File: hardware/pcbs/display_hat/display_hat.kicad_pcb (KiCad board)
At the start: 2 copper layers, 31 x 65 mm, 13 parts, among them J1 WAVESHARE_HAT_HEADER, J2 MTA100_08, J3 MTA100_08, J4 MTA100_02

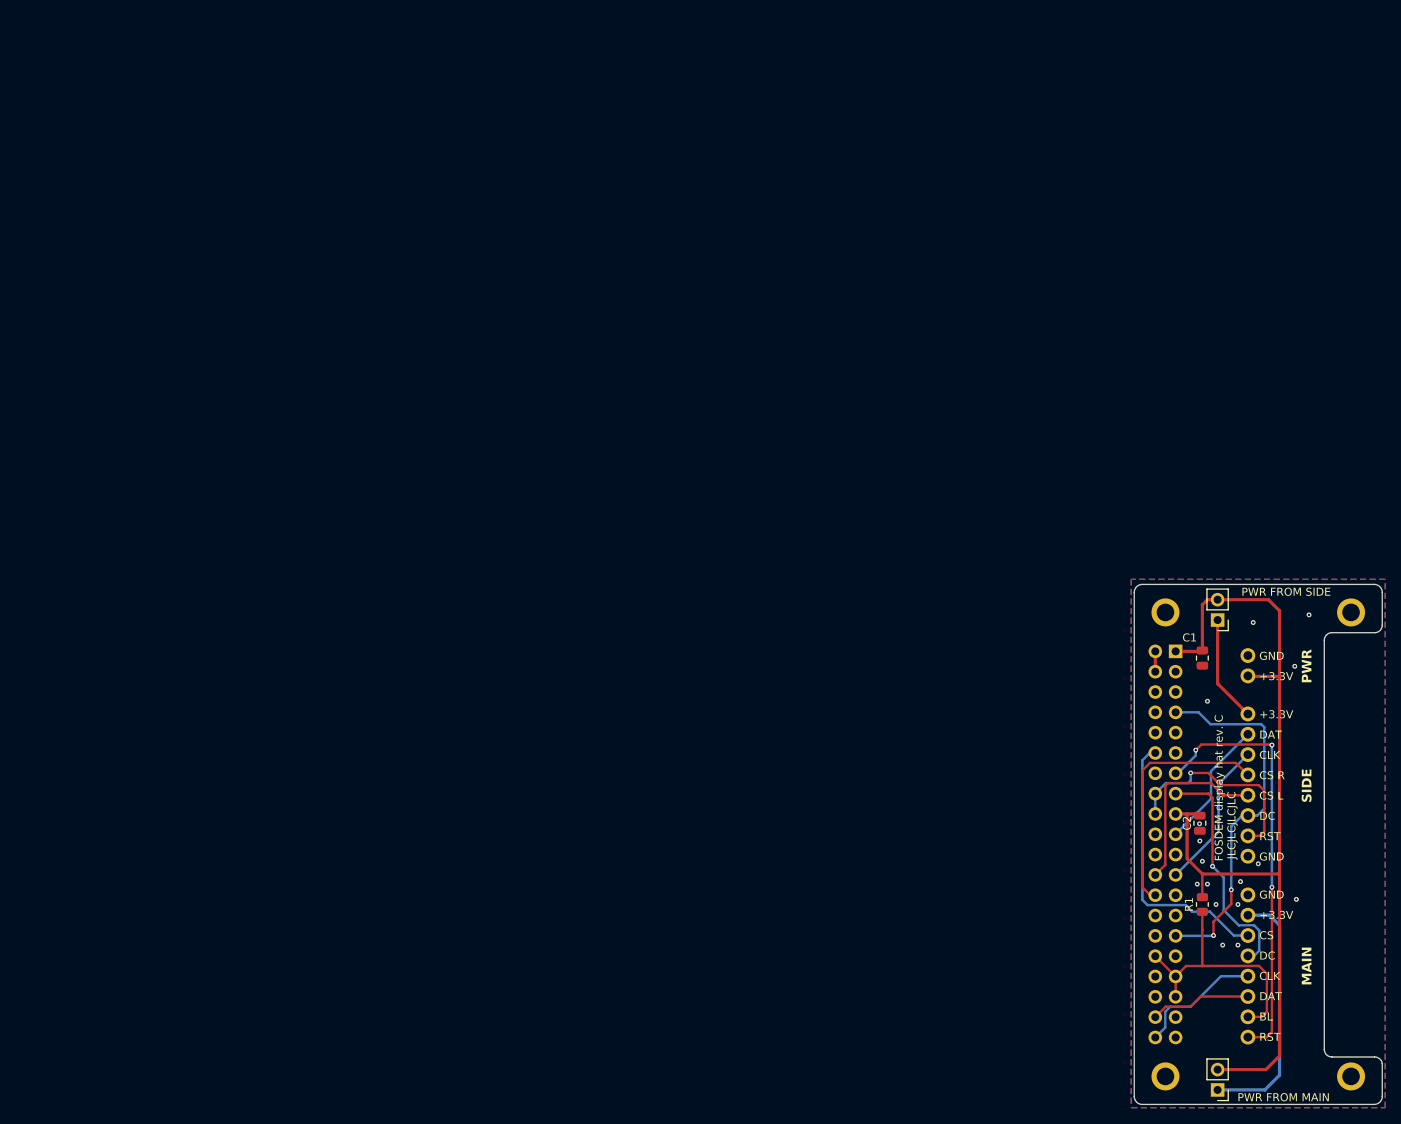
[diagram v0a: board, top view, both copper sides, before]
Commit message: baseplate: show 3D models of hat PCBs
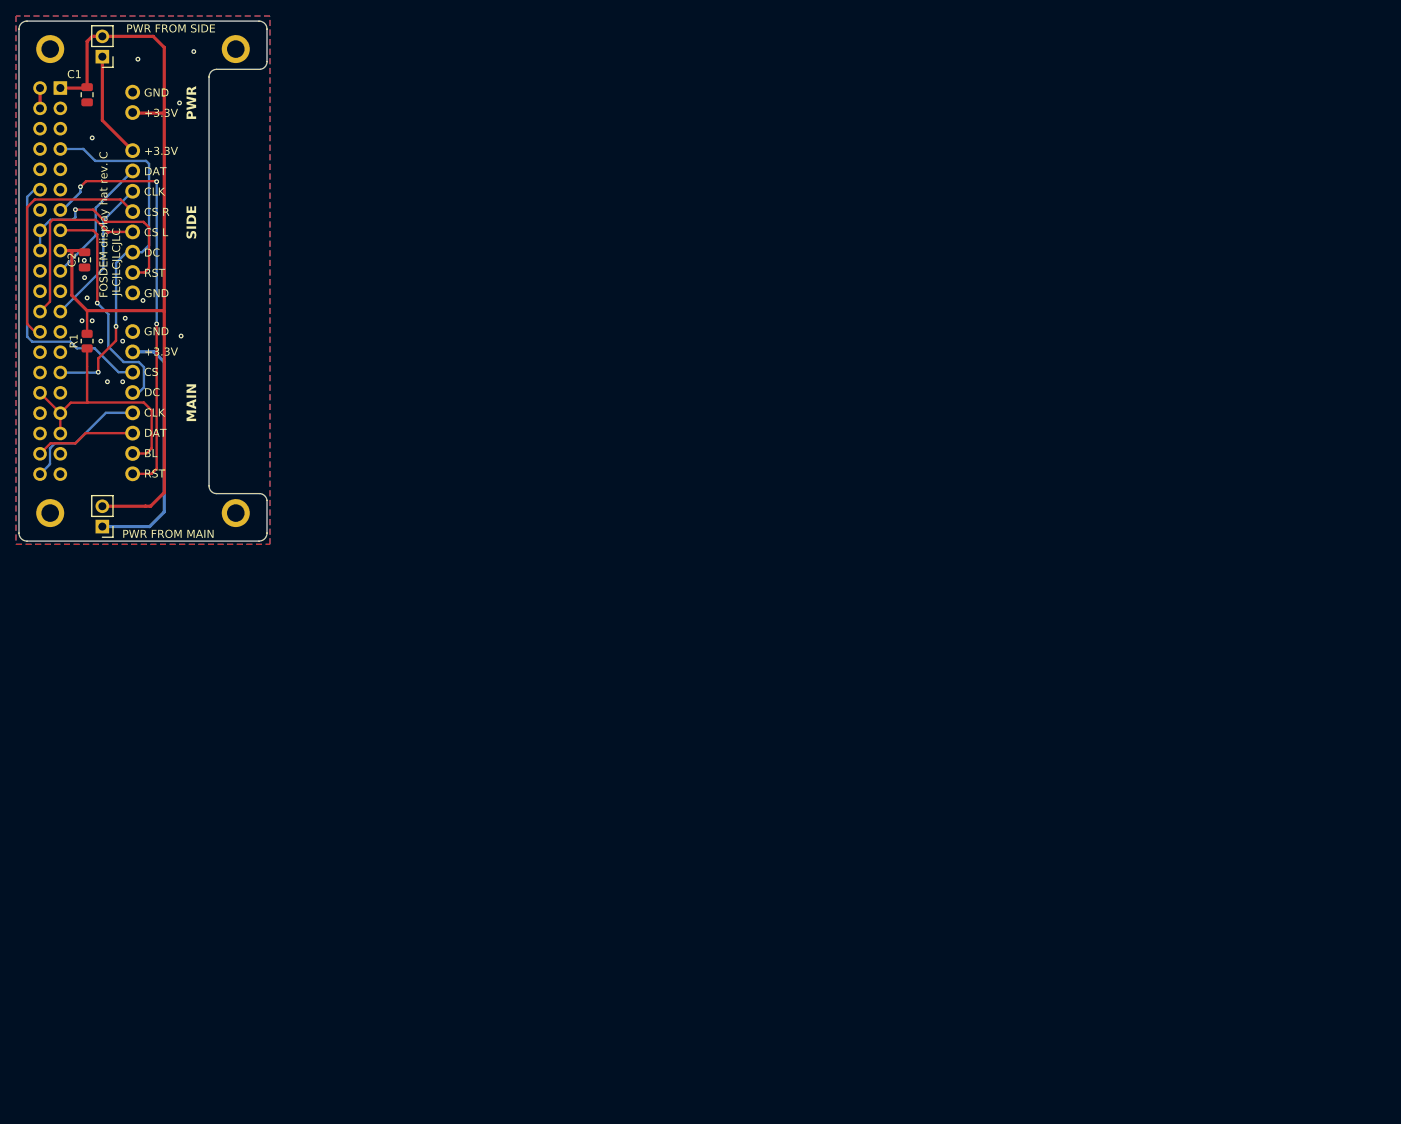
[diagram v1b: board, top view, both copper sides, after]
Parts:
- moved C1 156.2 mm to (4.62, 5.71)
- moved C2 156.2 mm to (4.30, 26.3)
- moved H1 156.2 mm to (23.2, 58.0)
- moved H2 156.2 mm to (0.00, 0.00)
- moved H3 156.2 mm to (23.2, 0.00)
- moved H4 156.2 mm to (0.00, 58.0)
- moved J1 156.2 mm to (1.27, 4.87)
- moved J2 156.2 mm to (10.3, 12.7)
- moved J3 156.2 mm to (10.3, 35.3)
- moved J4 156.2 mm to (10.3, 5.39)
- moved JP1 156.2 mm to (6.52, 0.95)
- moved JP2 156.2 mm to (6.52, 59.7)
- moved R1 156.2 mm to (4.62, 36.5)

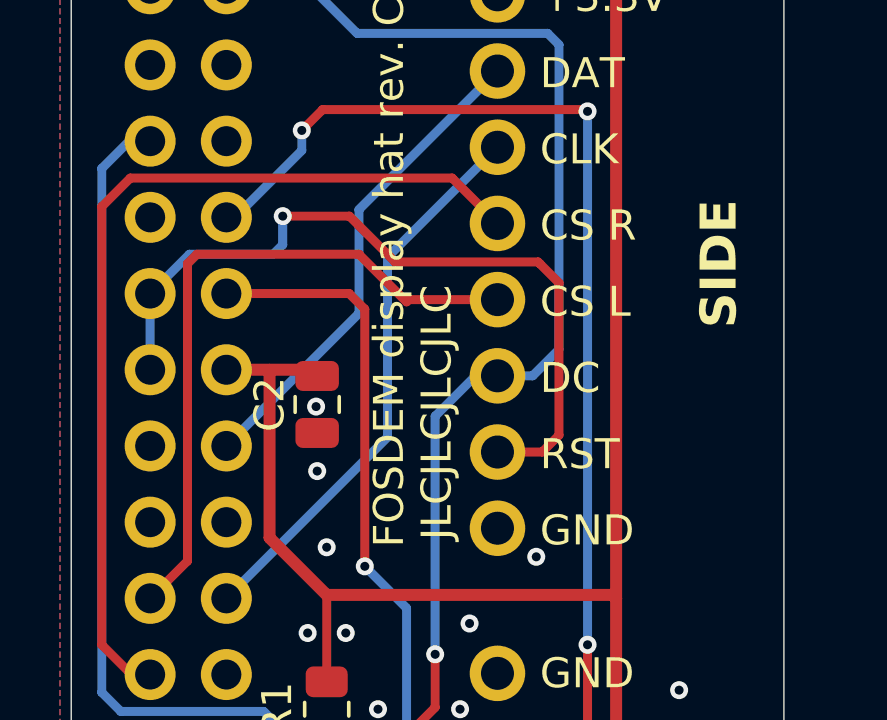
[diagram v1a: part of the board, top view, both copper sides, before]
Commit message: boards: fix minor mistakes and aisler IDs
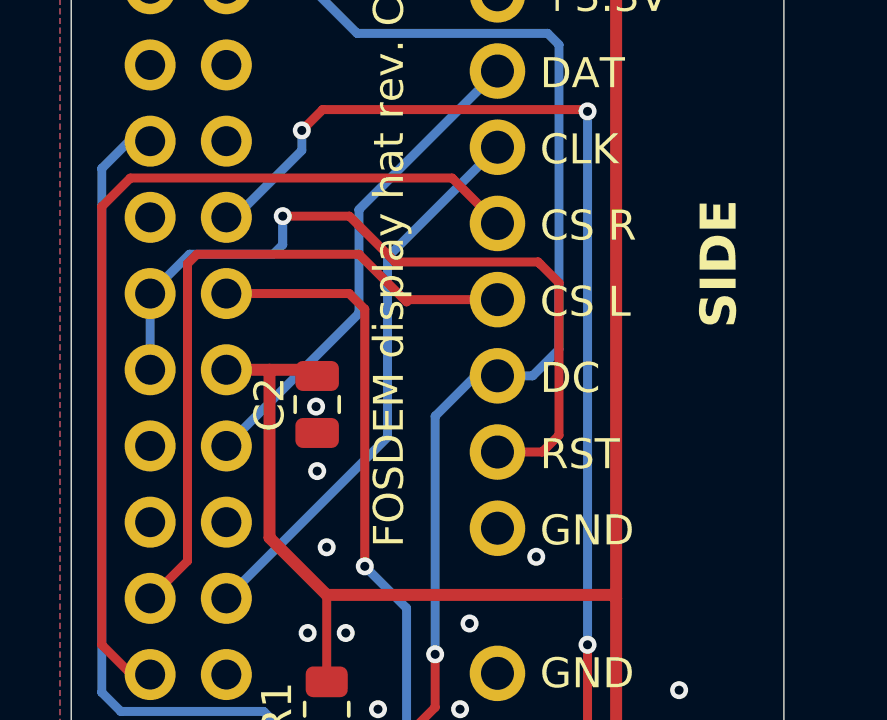
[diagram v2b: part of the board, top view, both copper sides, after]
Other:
- board text removed: "JLCJLCJLCJLC"
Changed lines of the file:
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@@
 		(layer "Edge.Cuts")
-	)
-	(gr_text "JLCJLCJLCJLC"
-		(at 8.865 30.865 90)
-		(layer "F.SilkS")
-		(effects
-			(font
-				(size 1 1)
-				(thickness 0.1)
-			)
-			(justify left bottom)
-		)
 	)
 	(gr_text "DAT"

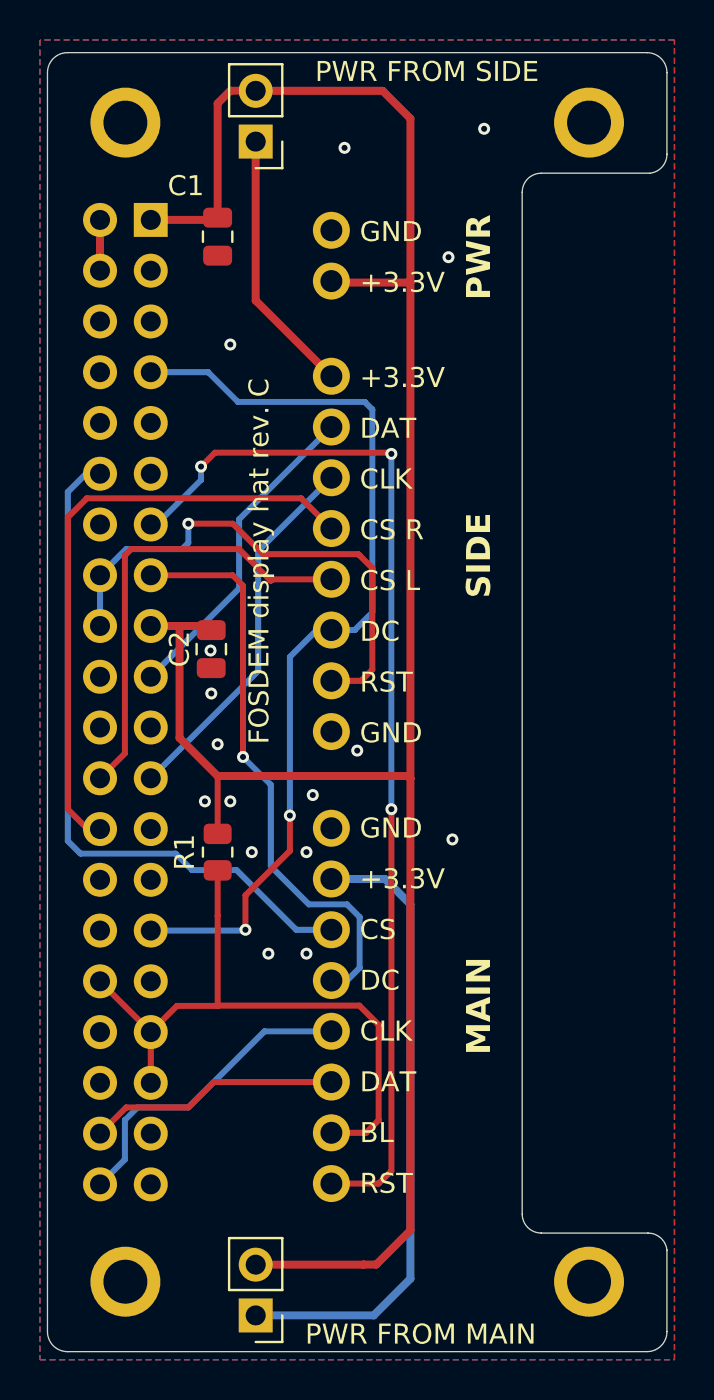
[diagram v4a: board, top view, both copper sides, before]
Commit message: hat_pcbs: more space under MTA100 connectors as per datasheet
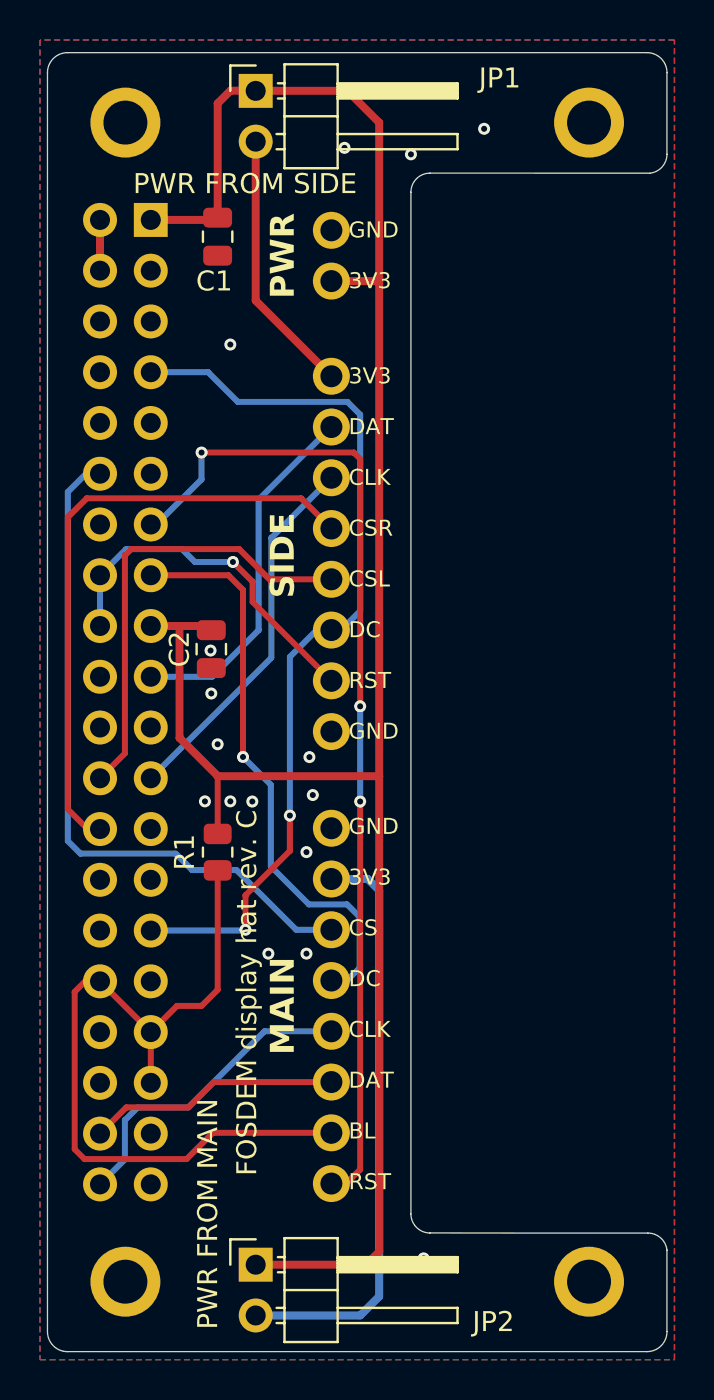
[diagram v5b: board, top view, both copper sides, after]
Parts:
- JP1, JP2: footprint Connector_PinHeader_2.54mm:PinHeader_1x02_P2.54mm_Vertical -> Connector_PinHeader_2.54mm:PinHeader_1x02_P2.54mm_Horizontal
- moved JP2 2.54 mm to (6.52, 57.1), turned to 0 degrees
- moved JP1 2.54 mm to (6.52, -1.59), turned to 0 degrees
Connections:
- JP1 pad 1: Net-(J2-Pin_8) -> +3.3V
- JP1 pad 2: +3.3V -> Net-(J2-Pin_8)
- JP2 pad 1: Net-(J3-Pin_7) -> +3.3V
- JP2 pad 2: +3.3V -> Net-(J3-Pin_7)
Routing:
- net /SIDE_RST: track 26.1 -> 18.0 mm
- net /BL: track 32.7 -> 39.3 mm
- net +3.3V: track 111.7 -> 106.0 mm
- net /MAIN_RST: track 53.1 -> 50.2 mm
- net Net-(J3-Pin_7): track 31.7 -> 29.5 mm
- net /SIDE_DAT: track 16.2 -> 18.0 mm
- net /SIDE_DC: track 46.4 -> 45.0 mm
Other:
- outline, holes or cut-outs redrawn
- board text added: "3V3"
- board text added: "CSL"
- board text added: "CSR"
- board text removed: "+3.3V"
- board text removed: "CS L"
- board text removed: "CS R"
